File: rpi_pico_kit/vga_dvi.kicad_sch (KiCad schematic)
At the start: 32 parts

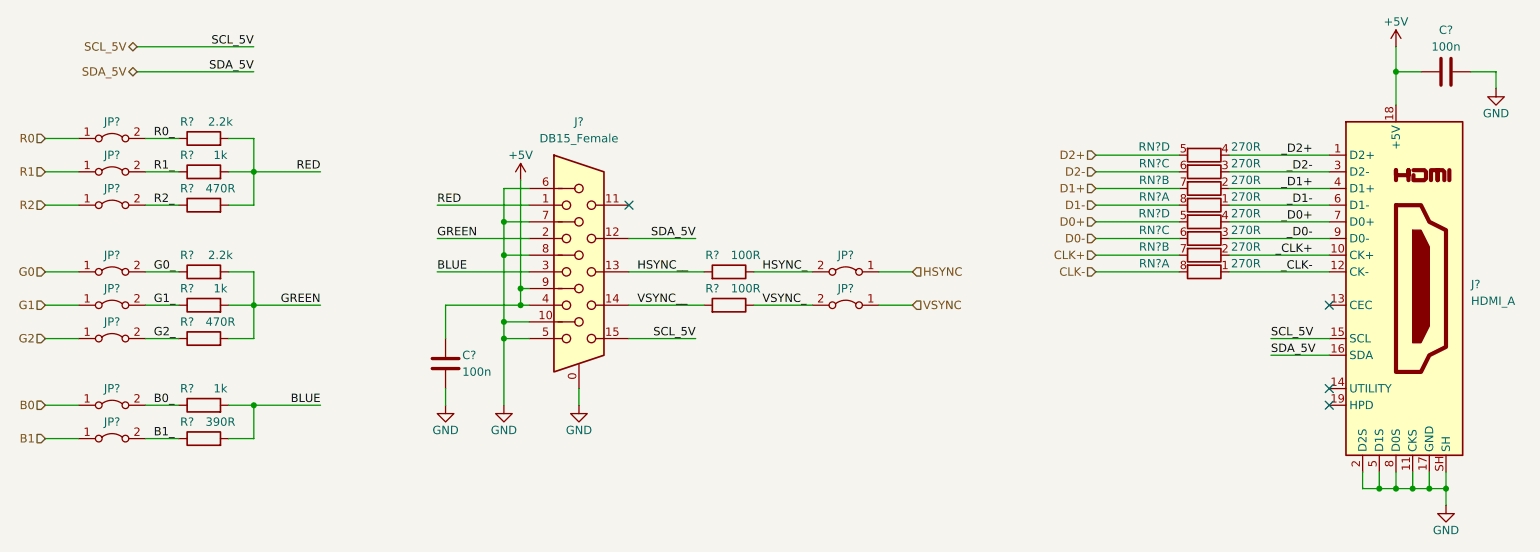
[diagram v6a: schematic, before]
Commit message: renumbered parts
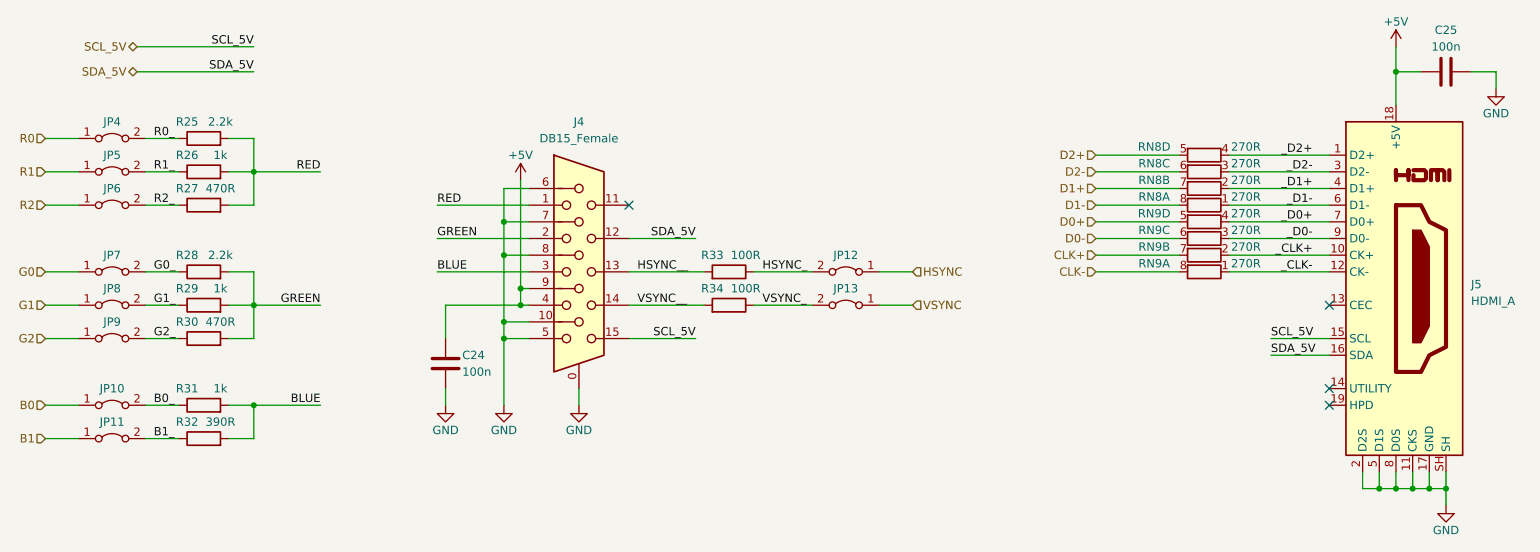
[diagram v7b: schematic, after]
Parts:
- gave numbers to parts that had none: 26
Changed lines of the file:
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@@
   (symbol (lib_id "Device:C") (at 251.46 59.69 90) (unit 1)
     (in_bom yes) (on_board yes)
-    (property "Reference" "C?" (id 0) (at 251.46 53.34 90)
+    (property "Reference" "C25" (id 0) (at 251.46 53.34 90)
       (effects (font (size 1.27 1.27)))
     )
@@
   (symbol (lib_id "Jumper:Jumper_2_Bridged") (at 160.02 90.17 0) (mirror y) (unit 1)
     (in_bom yes) (on_board yes) (fields_autoplaced)
-    (property "Reference" "JP?" (id 0) (at 160.02 87.63 0)
+    (property "Reference" "JP12" (id 0) (at 160.02 87.63 0)
       (effects (font (size 1.27 1.27)))
     )
@@
   (symbol (lib_id "Device:R") (at 62.23 100.33 90) (unit 1)
     (in_bom yes) (on_board yes)
-    (property "Reference" "R?" (id 0) (at 59.69 97.79 90)
+    (property "Reference" "R30" (id 0) (at 59.69 97.79 90)
       (effects (font (size 1.27 1.27)))
     )
@@
   (symbol (lib_id "Device:R_Pack04_Split") (at 214.63 90.17 90) (unit 1)
     (in_bom yes) (on_board yes)
-    (property "Reference" "RN?" (id 0) (at 207.01 88.9 90)
+    (property "Reference" "RN9" (id 0) (at 207.01 88.9 90)
       (effects (font (size 1.27 1.27)))
     )
@@
   (symbol (lib_id "Device:R") (at 62.23 95.25 90) (unit 1)
     (in_bom yes) (on_board yes)
-    (property "Reference" "R?" (id 0) (at 59.69 92.71 90)
+    (property "Reference" "R29" (id 0) (at 59.69 92.71 90)
       (effects (font (size 1.27 1.27)))
     )
@@
   (symbol (lib_id "Device:R") (at 142.24 95.25 270) (mirror x) (unit 1)
     (in_bom yes) (on_board yes)
-    (property "Reference" "R?" (id 0) (at 139.7 92.71 90)
+    (property "Reference" "R34" (id 0) (at 139.7 92.71 90)
       (effects (font (size 1.27 1.27)))
     )
@@
   (symbol (lib_id "Device:R_Pack04_Split") (at 214.63 74.93 90) (unit 3)
     (in_bom yes) (on_board yes)
-    (property "Reference" "RN?" (id 0) (at 207.01 73.66 90)
+    (property "Reference" "RN8" (id 0) (at 207.01 73.66 90)
       (effects (font (size 1.27 1.27)))
     )
@@
   (symbol (lib_id "Device:R") (at 62.23 69.85 90) (unit 1)
     (in_bom yes) (on_board yes)
-    (property "Reference" "R?" (id 0) (at 59.69 67.31 90)
+    (property "Reference" "R25" (id 0) (at 59.69 67.31 90)
       (effects (font (size 1.27 1.27)))
     )
@@
   (symbol (lib_id "Connector:DB15_Female_HighDensity_MountingHoles") (at 119.38 90.17 0) (unit 1)
     (in_bom yes) (on_board yes)
-    (property "Reference" "J?" (id 0) (at 119.38 67.31 0)
+    (property "Reference" "J4" (id 0) (at 119.38 67.31 0)
       (effects (font (size 1.27 1.27)))
     )
@@
   (symbol (lib_id "Jumper:Jumper_2_Bridged") (at 48.26 115.57 0) (unit 1)
     (in_bom yes) (on_board yes) (fields_autoplaced)
-    (property "Reference" "JP?" (id 0) (at 48.26 113.03 0)
+    (property "Reference" "JP11" (id 0) (at 48.26 113.03 0)
       (effects (font (size 1.27 1.27)))
     )
@@
   (symbol (lib_id "Device:R") (at 62.23 110.49 90) (unit 1)
     (in_bom yes) (on_board yes)
-    (property "Reference" "R?" (id 0) (at 59.69 107.95 90)
+    (property "Reference" "R31" (id 0) (at 59.69 107.95 90)
       (effects (font (size 1.27 1.27)))
     )
@@
   (symbol (lib_id "Jumper:Jumper_2_Bridged") (at 48.26 95.25 0) (unit 1)
     (in_bom yes) (on_board yes) (fields_autoplaced)
-    (property "Reference" "JP?" (id 0) (at 48.26 92.71 0)
+    (property "Reference" "JP8" (id 0) (at 48.26 92.71 0)
       (effects (font (size 1.27 1.27)))
     )
@@
   (symbol (lib_id "Device:R") (at 62.23 80.01 90) (unit 1)
     (in_bom yes) (on_board yes)
-    (property "Reference" "R?" (id 0) (at 59.69 77.47 90)
+    (property "Reference" "R27" (id 0) (at 59.69 77.47 90)
       (effects (font (size 1.27 1.27)))
     )
@@
   (symbol (lib_id "Device:C") (at 99.06 104.14 180) (unit 1)
     (in_bom yes) (on_board yes)
-    (property "Reference" "C?" (id 0) (at 101.6 102.87 0)
+    (property "Reference" "C24" (id 0) (at 101.6 102.87 0)
       (effects (font (size 1.27 1.27)) (justify right))
     )
@@
   (symbol (lib_id "Jumper:Jumper_2_Bridged") (at 48.26 100.33 0) (unit 1)
     (in_bom yes) (on_board yes) (fields_autoplaced)
-    (property "Reference" "JP?" (id 0) (at 48.26 97.79 0)
+    (property "Reference" "JP9" (id 0) (at 48.26 97.79 0)
       (effects (font (size 1.27 1.27)))
     )
@@
   (symbol (lib_id "Jumper:Jumper_2_Bridged") (at 48.26 80.01 0) (unit 1)
     (in_bom yes) (on_board yes) (fields_autoplaced)
-    (property "Reference" "JP?" (id 0) (at 48.26 77.47 0)
+    (property "Reference" "JP6" (id 0) (at 48.26 77.47 0)
       (effects (font (size 1.27 1.27)))
     )
@@
   (symbol (lib_id "Jumper:Jumper_2_Bridged") (at 48.26 69.85 0) (unit 1)
     (in_bom yes) (on_board yes) (fields_autoplaced)
-    (property "Reference" "JP?" (id 0) (at 48.26 67.31 0)
+    (property "Reference" "JP4" (id 0) (at 48.26 67.31 0)
       (effects (font (size 1.27 1.27)))
     )
@@
   (symbol (lib_id "Device:R_Pack04_Split") (at 214.63 87.63 90) (unit 2)
     (in_bom yes) (on_board yes)
-    (property "Reference" "RN?" (id 0) (at 207.01 86.36 90)
+    (property "Reference" "RN9" (id 0) (at 207.01 86.36 90)
       (effects (font (size 1.27 1.27)))
     )
@@
   (symbol (lib_id "Device:R") (at 62.23 90.17 90) (unit 1)
     (in_bom yes) (on_board yes)
-    (property "Reference" "R?" (id 0) (at 59.69 87.63 90)
+    (property "Reference" "R28" (id 0) (at 59.69 87.63 90)
       (effects (font (size 1.27 1.27)))
     )
@@
   (symbol (lib_id "Device:R") (at 62.23 74.93 90) (unit 1)
     (in_bom yes) (on_board yes)
-    (property "Reference" "R?" (id 0) (at 59.69 72.39 90)
+    (property "Reference" "R26" (id 0) (at 59.69 72.39 90)
       (effects (font (size 1.27 1.27)))
     )
@@
   (symbol (lib_id "Connector:HDMI_A") (at 243.84 92.71 0) (unit 1)
     (in_bom yes) (on_board yes) (fields_autoplaced)
-    (property "Reference" "J?" (id 0) (at 255.27 92.075 0)
+    (property "Reference" "J5" (id 0) (at 255.27 92.075 0)
       (effects (font (size 1.27 1.27)) (justify left))
     )
@@
   (symbol (lib_id "Jumper:Jumper_2_Bridged") (at 160.02 95.25 0) (mirror y) (unit 1)
     (in_bom yes) (on_board yes) (fields_autoplaced)
-    (property "Reference" "JP?" (id 0) (at 160.02 92.71 0)
+    (property "Reference" "JP13" (id 0) (at 160.02 92.71 0)
       (effects (font (size 1.27 1.27)))
     )
@@
   (symbol (lib_id "Device:R_Pack04_Split") (at 214.63 85.09 90) (unit 3)
     (in_bom yes) (on_board yes)
-    (property "Reference" "RN?" (id 0) (at 207.01 83.82 90)
+    (property "Reference" "RN9" (id 0) (at 207.01 83.82 90)
       (effects (font (size 1.27 1.27)))
     )
@@
   (symbol (lib_id "Jumper:Jumper_2_Bridged") (at 48.26 74.93 0) (unit 1)
     (in_bom yes) (on_board yes) (fields_autoplaced)
-    (property "Reference" "JP?" (id 0) (at 48.26 72.39 0)
+    (property "Reference" "JP5" (id 0) (at 48.26 72.39 0)
       (effects (font (size 1.27 1.27)))
     )
@@
   (symbol (lib_id "Jumper:Jumper_2_Bridged") (at 48.26 110.49 0) (unit 1)
     (in_bom yes) (on_board yes) (fields_autoplaced)
-    (property "Reference" "JP?" (id 0) (at 48.26 107.95 0)
+    (property "Reference" "JP10" (id 0) (at 48.26 107.95 0)
       (effects (font (size 1.27 1.27)))
     )
@@
   (symbol (lib_id "Device:R") (at 142.24 90.17 270) (mirror x) (unit 1)
     (in_bom yes) (on_board yes)
-    (property "Reference" "R?" (id 0) (at 139.7 87.63 90)
+    (property "Reference" "R33" (id 0) (at 139.7 87.63 90)
       (effects (font (size 1.27 1.27)))
     )
@@
   (symbol (lib_id "Device:R_Pack04_Split") (at 214.63 77.47 90) (unit 2)
     (in_bom yes) (on_board yes)
-    (property "Reference" "RN?" (id 0) (at 207.01 76.2 90)
+    (property "Reference" "RN8" (id 0) (at 207.01 76.2 90)
       (effects (font (size 1.27 1.27)))
     )
@@
   (symbol (lib_id "Device:R_Pack04_Split") (at 214.63 72.39 90) (unit 4)
     (in_bom yes) (on_board yes)
-    (property "Reference" "RN?" (id 0) (at 207.01 71.12 90)
+    (property "Reference" "RN8" (id 0) (at 207.01 71.12 90)
       (effects (font (size 1.27 1.27)))
     )
@@
   (symbol (lib_id "Device:R") (at 62.23 115.57 90) (unit 1)
     (in_bom yes) (on_board yes)
-    (property "Reference" "R?" (id 0) (at 59.69 113.03 90)
+    (property "Reference" "R32" (id 0) (at 59.69 113.03 90)
       (effects (font (size 1.27 1.27)))
     )
@@
   (symbol (lib_id "Device:R_Pack04_Split") (at 214.63 82.55 90) (unit 4)
     (in_bom yes) (on_board yes)
-    (property "Reference" "RN?" (id 0) (at 207.01 81.28 90)
+    (property "Reference" "RN9" (id 0) (at 207.01 81.28 90)
       (effects (font (size 1.27 1.27)))
     )
@@
   (symbol (lib_id "Jumper:Jumper_2_Bridged") (at 48.26 90.17 0) (unit 1)
     (in_bom yes) (on_board yes) (fields_autoplaced)
-    (property "Reference" "JP?" (id 0) (at 48.26 87.63 0)
+    (property "Reference" "JP7" (id 0) (at 48.26 87.63 0)
       (effects (font (size 1.27 1.27)))
     )
@@
   (symbol (lib_id "Device:R_Pack04_Split") (at 214.63 80.01 90) (unit 1)
     (in_bom yes) (on_board yes)
-    (property "Reference" "RN?" (id 0) (at 207.01 78.74 90)
-      (effects (font (size 1.27 1.27)))
-    )
+    (property "Reference" "RN8" (id 0) (at 207.01 78.74 90)
+      (effects (font (size 1.27 1.27)))
+    )
